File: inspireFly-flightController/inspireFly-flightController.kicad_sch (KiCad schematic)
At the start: 74 parts, among them J1 FTSH-107-01-L-DV-K-A, SW1 SW_Push, SW3 SW_Push, U1 STM32U595VJT6, U2 BNO086, U3 RV-8803-C7, U4 LM66100DCK, U5 TPS2117, U6 RV-8803-C7, U7 MX60LF8G28AD-TI, Y1 ABS07-32.768KHZ-T, Y2 ABS07-32.768KHZ-T

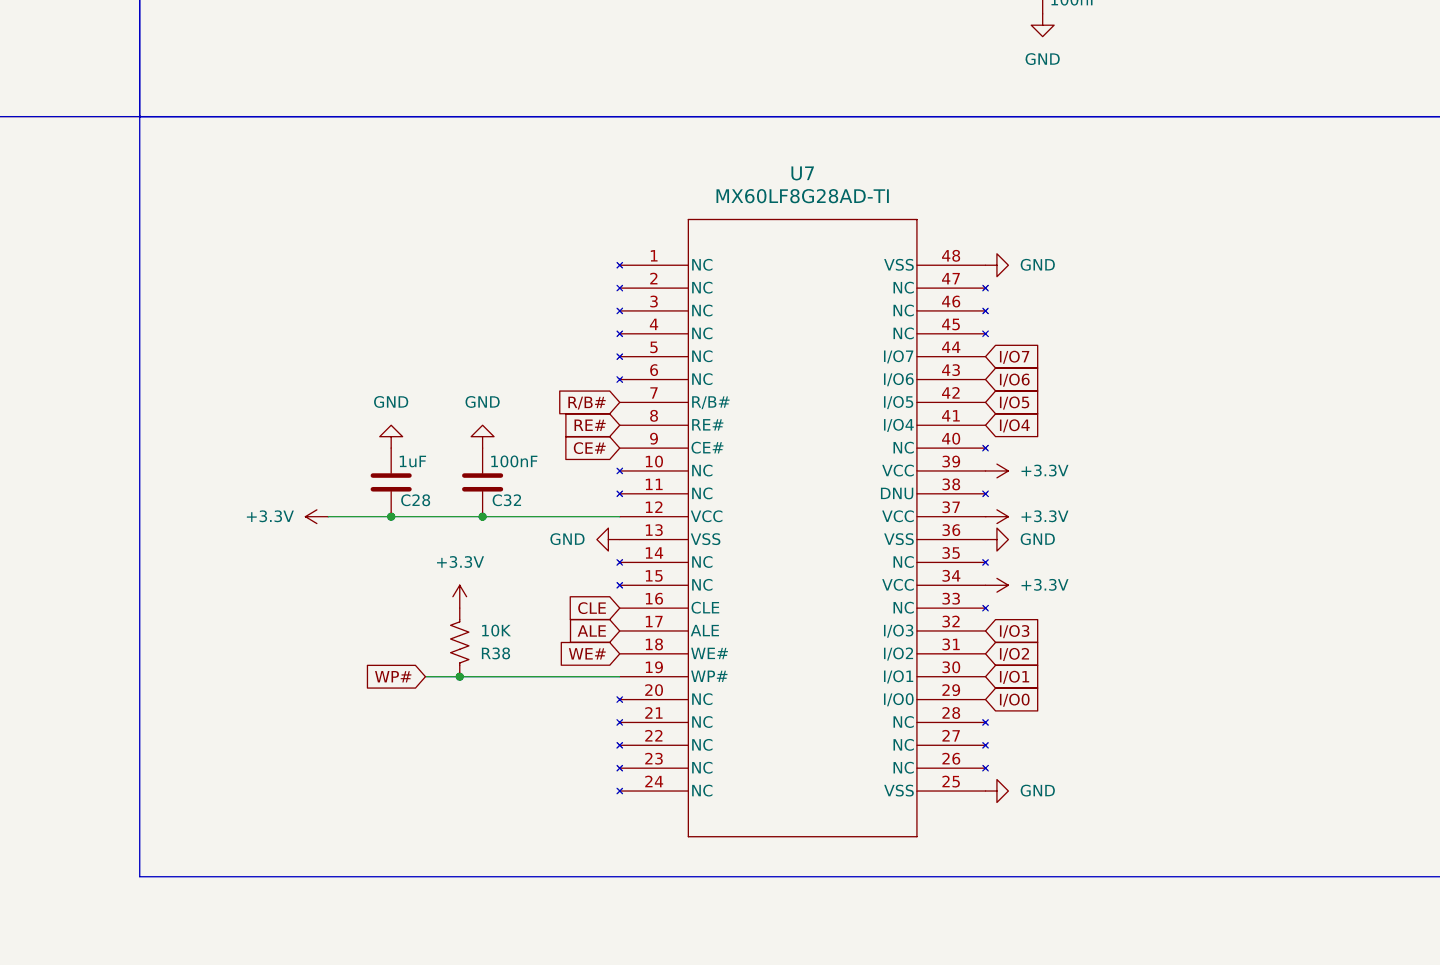
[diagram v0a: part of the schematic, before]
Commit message: Updated 1GB flash storage IC schematic
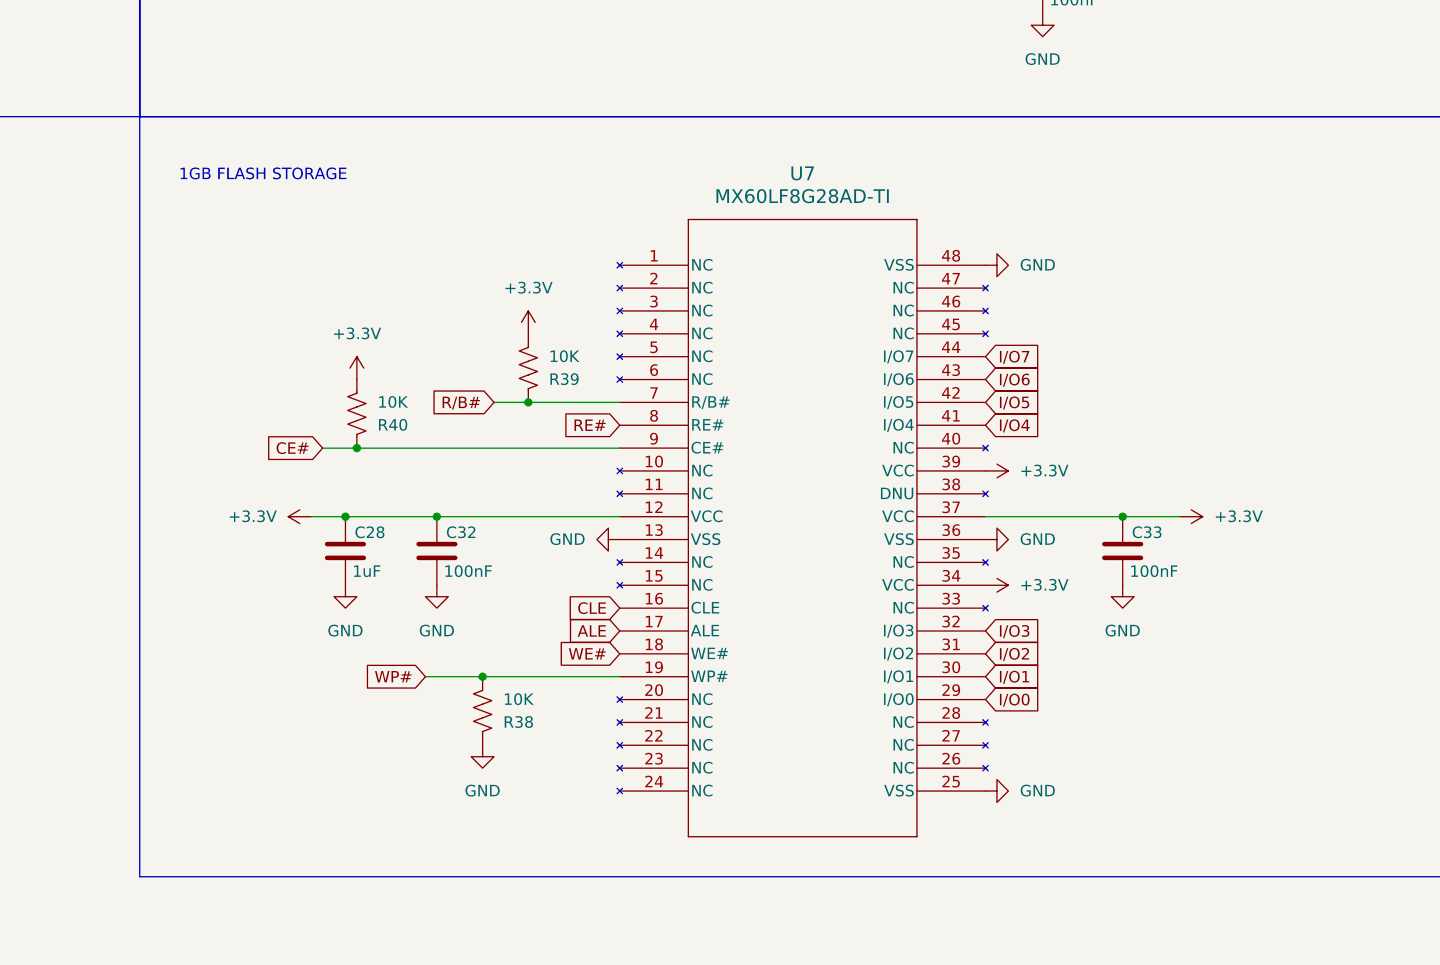
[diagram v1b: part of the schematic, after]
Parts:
- added C33: 100nF, Capacitor_SMD:C_0402_1005Metric_Pad0.74x0.62mm_HandSolder, symbol Device:C
- added R39, R40: 10K, Resistor_SMD:R_0402_1005Metric_Pad0.72x0.64mm_HandSolder, symbol Device:R_US
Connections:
- net +3.3V: now also C33.1, R39.2, R40.2; no longer R38.2
- net CE#: now also R40.1
- net GND: now also R38.1, C33.2
- net R/B#: now also R39.1
- net WP#: now also R38.2; no longer R38.1
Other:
- note added: "1GB FLASH STORAGE"
- moved on the sheet: C28, C32, R38

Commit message: sync PCB with schematic
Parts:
- removed C21, C31: 1.5F, inspirefly:SUPERCAP_KR-5R5H155-R, symbol Device:C_Polarized
- removed R18, R7: 4.7k, Resistor_SMD:R_0402_1005Metric_Pad0.72x0.64mm_HandSolder, symbol Device:R_US
- removed TP2: VCAP_A2, TestPoint:TestPoint_Pad_D1.5mm, symbol Connector:TestPoint
- removed TP8: VCAP_B2, TestPoint:TestPoint_Pad_D1.5mm, symbol Connector:TestPoint
- TP1: value VACP_A1 -> VCAP_A1

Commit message: Slight tweaks to 1GB flash storage schematic
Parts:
- added C21, C31: 1.5F, inspirefly:SUPERCAP_KR-5R5H155-R, symbol Device:C_Polarized
- added R18, R7: 4.7k, Resistor_SMD:R_0402_1005Metric_Pad0.72x0.64mm_HandSolder, symbol Device:R_US
- added TP2: VCAP_A2, TestPoint:TestPoint_Pad_D1.5mm, symbol Connector:TestPoint
- added TP8: VCAP_B2, TestPoint:TestPoint_Pad_D1.5mm, symbol Connector:TestPoint
- R39: value 10K -> 4.7K
- TP1: value VCAP_A1 -> VACP_A1
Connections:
- net GND: now also C21.2, C31.2
- net VRTC_A: now also R7.2
- net VRTC_B: now also R18.2
- new net VCAP_A2: C21.1, R7.1, TP2.1
- new net VCAP_B2: C31.1, R18.1, TP8.1

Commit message: Interfaced 1GB flash storage IC onto PCB, updated footprints
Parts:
- U7: footprint TSOPI48_MAC -> Flash_Storage:TSOPI48_MAC
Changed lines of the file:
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@@
 			)
 		)
-		(property "Footprint" "TSOPI48_MAC"
+		(property "Footprint" "Flash_Storage:TSOPI48_MAC"
 			(at 318.77 101.6 0)
 			(hide yes)

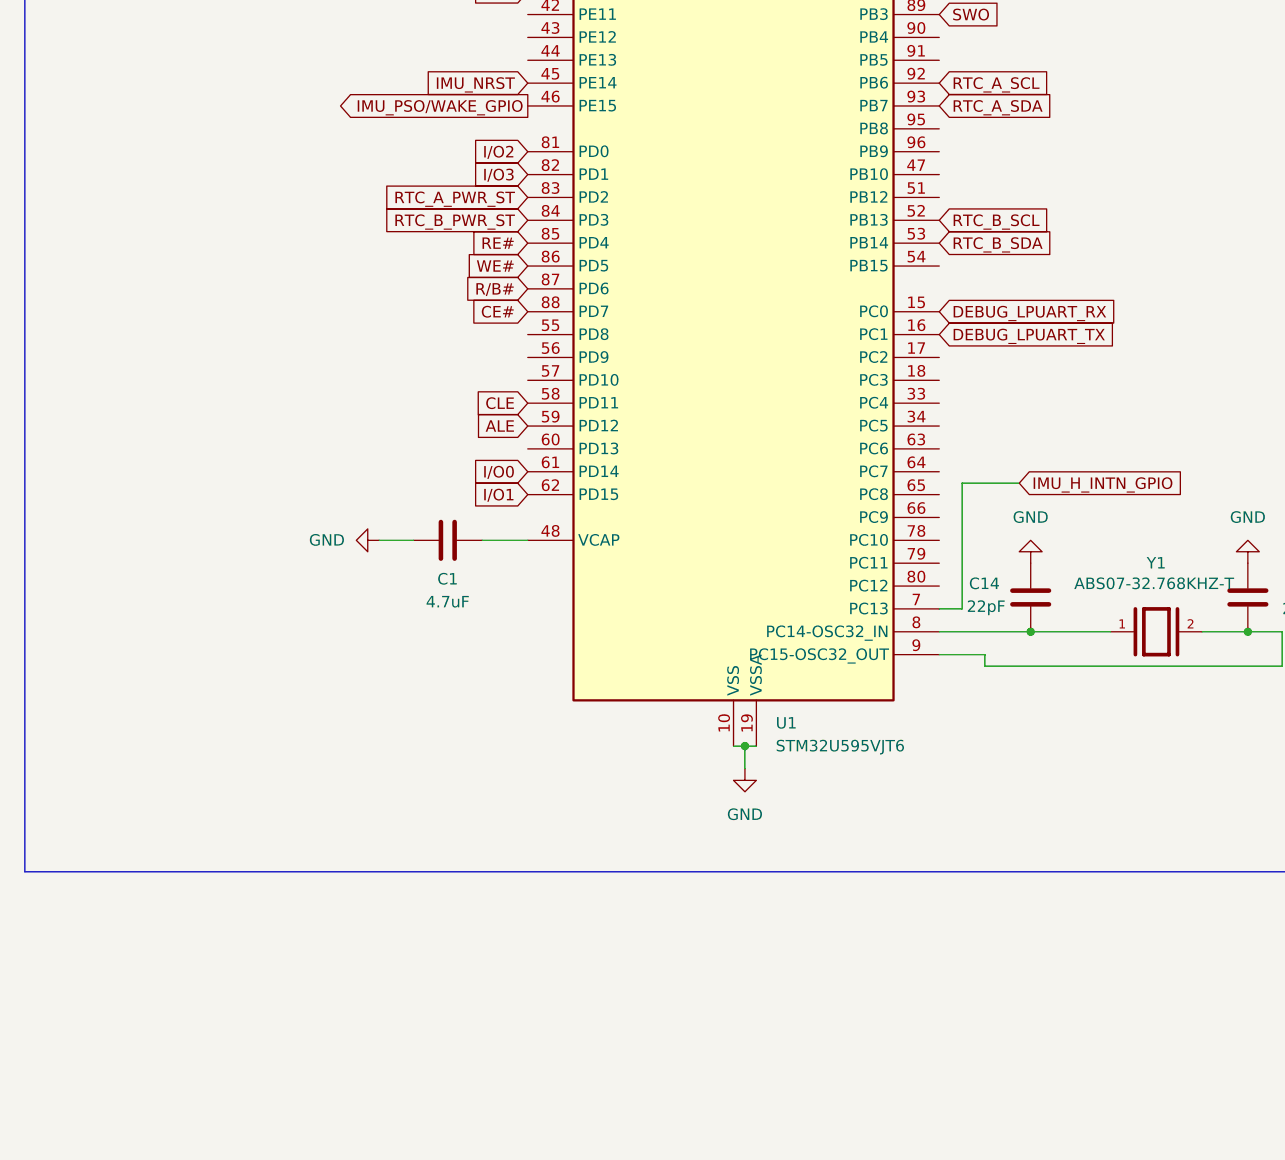
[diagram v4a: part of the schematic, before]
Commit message: added door sending
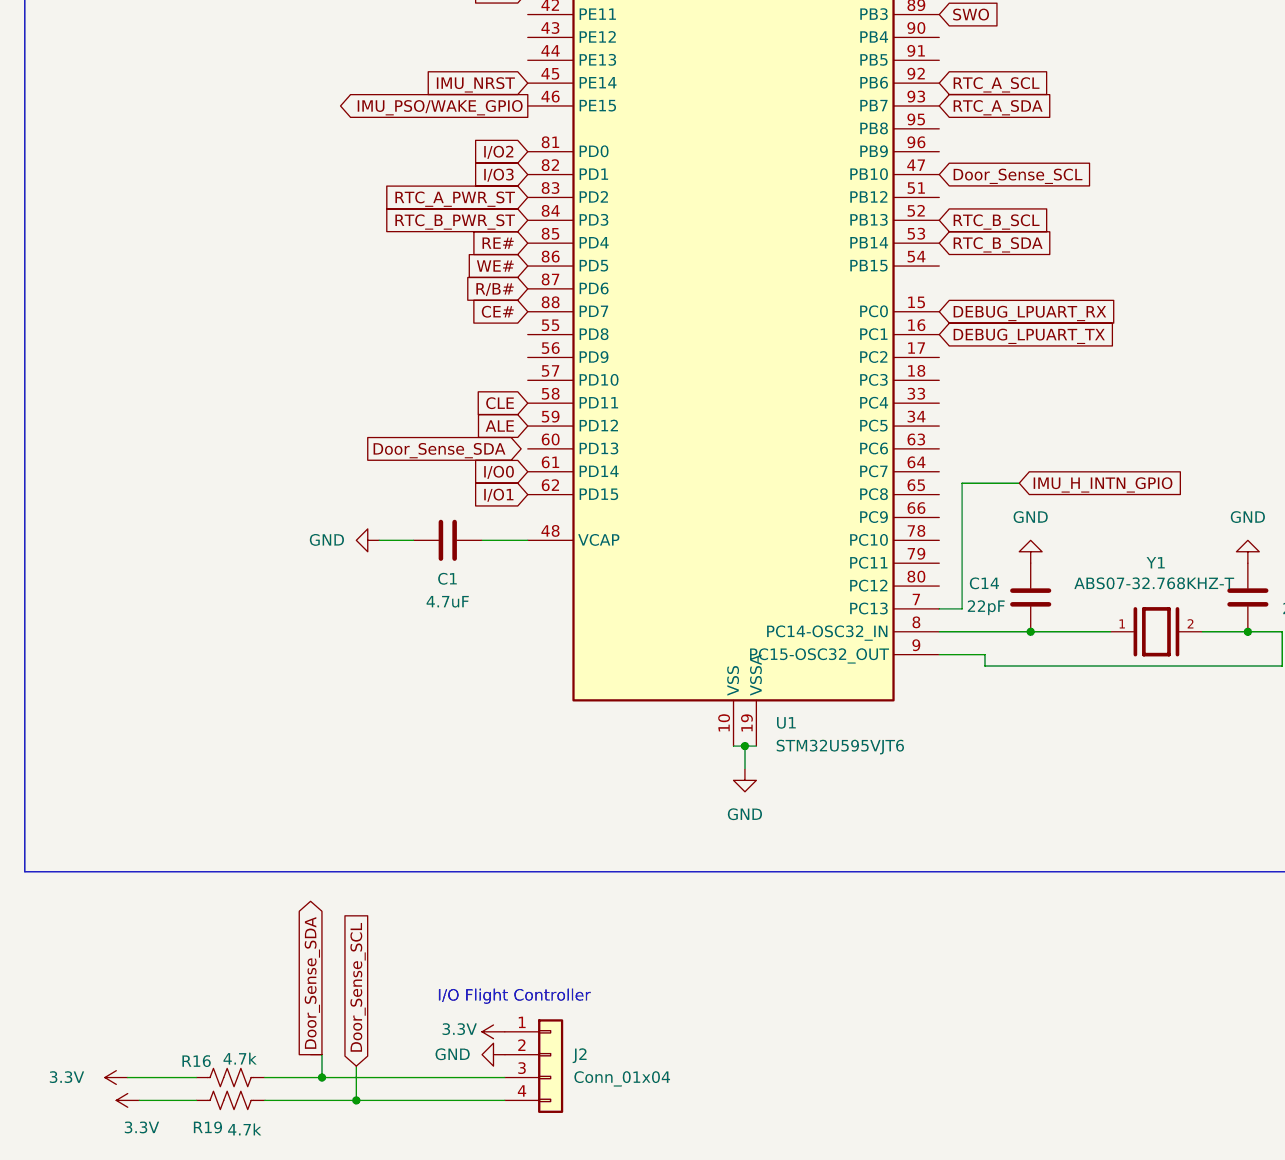
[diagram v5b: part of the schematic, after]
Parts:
- added J2: Conn_01x04, Connector_JST:JST_PH_S4B-PH-K_1x04_P2.00mm_Horizontal, symbol Connector_Generic:Conn_01x04
- added R16, R19: 4.7k, Resistor_SMD:R_0603_1608Metric, symbol Device:R_US
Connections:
- net GND: now also J2.2 (Pin_2)
- net Door_Sense_SCL: now reaches U1.47 (PB10)
- net Door_Sense_SCL: now also J2.4 (Pin_4), R19.2
- new net 3.3V: J2.1 (Pin_1), R16.1, R19.1
- new net Door_Sense_SDA: J2.3 (Pin_3), R16.2
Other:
- note added: "I/O Flight Controller"

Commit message: added door sense enable to fc
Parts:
- removed J2: Conn_01x04, Connector_JST:JST_PH_S4B-PH-K_1x04_P2.00mm_Horizontal, symbol Connector_Generic:Conn_01x04
- added J2: Conn_01x05, symbol Connector_Generic:Conn_01x05
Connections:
- net 3.3V: now also J2.1 (Pin_1)
- net Door_Sense_SCL: now also J2.4 (Pin_4)
- net Door_Sense_SDA: now also J2.3 (Pin_3)
- net GND: now also J2.2 (Pin_2)
- net Door_sense_en: now reaches U1.51 (PB12)
- net Door_sense_en: now also J2.5 (Pin_5)
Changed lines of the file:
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@@
 		)
 	)
+	(text "I/O Flight Controller"
+		(exclude_from_sim no)
+		(at 83.312 209.804 0)
+		(effects
+			(font
+				(size 1.27 1.27)
+			)
+		)
+	)
 	(text "Ideal diode\n"
 		(exclude_from_sim no)
@@
 		)
 	)
+	(global_label "Door_sense_en"
+		(shape input)
+		(at 114.3 116.84 0)
+		(fields_autoplaced yes)
+		(effects
+			(font
+				(size 1.27 1.27)
+			)
+			(justify left)
+		)
+		(property "Intersheetrefs" "${INTERSHEET_REFS}"
+			(at 131.1946 116.84 0)
+			(hide yes)
+			(show_name no)
+			(do_not_autoplace no)
+			(effects
+				(font
+					(size 1.27 1.27)
+				)
+				(justify left)
+			)
+		)
+	)
 	(global_label "DEBUG_LPUART_RX"
 		(shape input)
@@
 		)
 	)
+	(global_label "Door_sense_en"
+		(shape input)
+		(at 66.04 219.71 180)
+		(fields_autoplaced yes)
+		(effects
+			(font
+				(size 1.27 1.27)
+			)
+			(justify right)
+		)
+		(property "Intersheetrefs" "${INTERSHEET_REFS}"
+			(at 49.1454 219.71 0)
+			(hide yes)
+			(show_name no)
+			(do_not_autoplace no)
+			(effects
+				(font
+					(size 1.27 1.27)
+				)
+				(justify right)
+			)
+		)
+	)
 	(global_label "Door_Sense_SDA"
 		(shape output)
@@
 	)
 	(symbol
+		(lib_id "Connector_Generic:Conn_01x05")
+		(at 71.12 214.63 0)
+		(unit 1)
+		(body_style 1)
+		(exclude_from_sim no)
+		(in_bom yes)
+		(on_board yes)
+		(in_pos_files yes)
+		(dnp no)
+		(fields_autoplaced yes)
+		(property "Reference" "J2"
+			(at 73.66 213.3599 0)
+			(show_name no)
+			(do_not_autoplace no)
+			(effects
+				(font
+					(size 1.27 1.27)
+				)
+				(justify left)
+			)
+		)
+		(property "Value" "Conn_01x05"
+			(at 73.66 215.8999 0)
+			(show_name no)
+			(do_not_autoplace no)
+			(effects
+				(font
+					(size 1.27 1.27)
+				)
+				(justify left)
+			)
+		)
+		(property "Footprint" ""
+			(at 71.12 214.63 0)
+			(hide yes)
+			(show_name no)
+			(do_not_autoplace no)
+			(effects
+				(font
+					(size 1.27 1.27)
+				)
+			)
+		)
+		(property "Datasheet" ""
+			(at 71.12 214.63 0)
+			(hide yes)
+			(show_name no)
+			(do_not_autoplace no)
+			(effects
+				(font
+					(size 1.27 1.27)
+				)
+			)
+		)
+		(property "Description" "Generic connector, single row, 01x05, script generated (kicad-library-utils/schlib/autogen/connector/)"
+			(at 71.12 214.63 0)
+			(hide yes)
+			(show_name no)
+			(do_not_autoplace no)
+			(effects
+				(font
+					(size 1.27 1.27)
+				)
+			)
+		)
+		(pin "5"
+		)
+		(pin "3"
+		)
+		(pin "2"
+		)
+		(pin "4"
+		)
+		(pin "1"
+		)
+		(instances
+			(project "inspireFly-flightController"
+				(path "/7e6c7bc0-1a4e-437f-8207-dca0e7985164"
+					(reference "J2")
+					(unit 1)
+				)
+			)
+		)
+	)
+	(symbol
 		(lib_id "power:GND")
 		(at 538.48 44.45 0)
@@
 					(unit 1)
 				)
-			)
-		)
-	)
-	(symbol
-		(lib_id "Connector_Generic:Conn_01x04")
-		(at 71.12 212.09 0)
-		(unit 1)
-		(body_style 1)
-		(exclude_from_sim no)
-		(in_bom yes)
-		(on_board yes)
-		(in_pos_files yes)
-		(dnp no)
-		(fields_autoplaced yes)
-		(property "Reference" "J2"
-			(at 73.66 212.0899 0)
-			(show_name no)
-			(do_not_autoplace no)
-			(effects
-				(font
-					(size 1.27 1.27)
-				)
-				(justify left)
-			)
-		)
-		(property "Value" "Conn_01x04"
-			(at 73.66 214.6299 0)
-			(show_name no)
-			(do_not_autoplace no)
-			(effects
-				(font
-					(size 1.27 1.27)
-				)
-				(justify left)
-			)
-		)
-		(property "Footprint" "Connector_JST:JST_PH_S4B-PH-K_1x04_P2.00mm_Horizontal"
-			(at 71.12 212.09 0)
-			(hide yes)
-			(show_name no)
-			(do_not_autoplace no)
-			(effects
-				(font
-					(size 1.27 1.27)
-				)
-			)
-		)
-		(property "Datasheet" ""
-			(at 71.12 212.09 0)
-			(hide yes)
-			(show_name no)
-			(do_not_autoplace no)
-			(effects
-				(font
-					(size 1.27 1.27)
-				)
-			)
-		)
-		(property "Description" "Generic connector, single row, 01x04, script generated (kicad-library-utils/schlib/autogen/connector/)"
-			(at 71.12 212.09 0)
-			(hide yes)
-			(show_name no)
-			(do_not_autoplace no)
-			(effects
-				(font
-					(size 1.27 1.27)
-				)
-			)
-		)
-		(pin "3"
-		)
-		(pin "4"
-		)
-		(pin "2"
-		)
-		(pin "1"
-		)
-		(instances
-			(project "inspireFly-flightController"
-				(path "/7e6c7bc0-1a4e-437f-8207-dca0e7985164"
-					(reference "J2")
-					(unit 1)
-				)
